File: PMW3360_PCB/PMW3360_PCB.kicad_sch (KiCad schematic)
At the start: 15 parts, among them J1 Conn_01x08, U1 PMW3360DM-T2QU, U2 TPS73601DBV

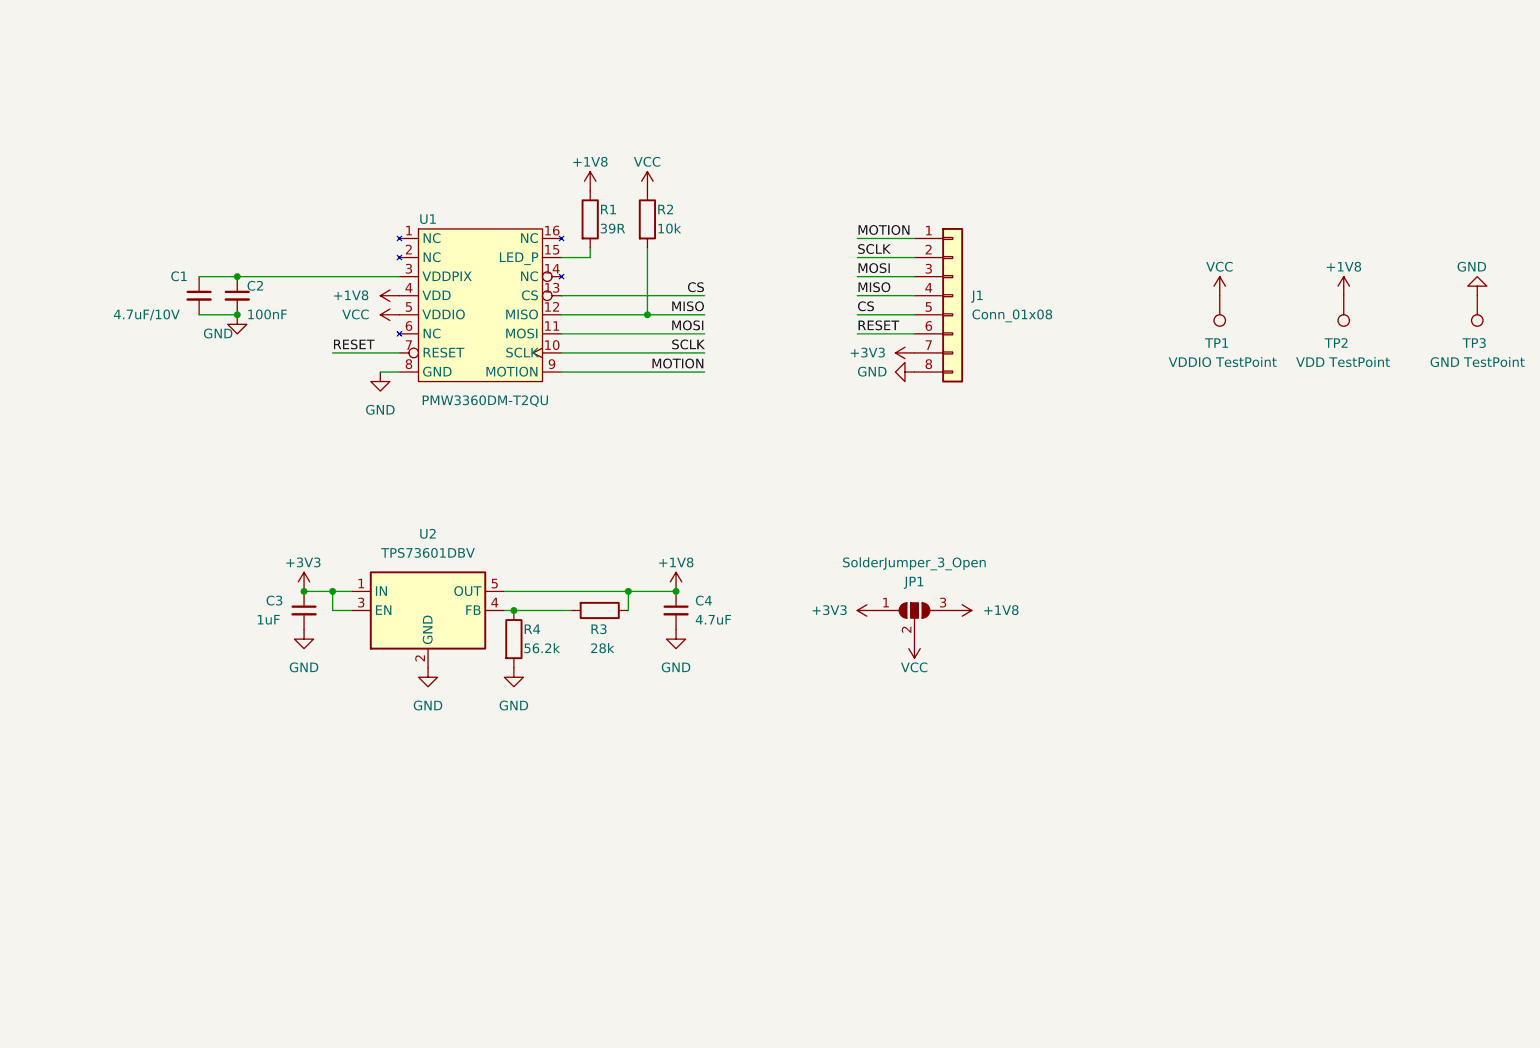
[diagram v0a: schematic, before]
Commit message: Update power net name
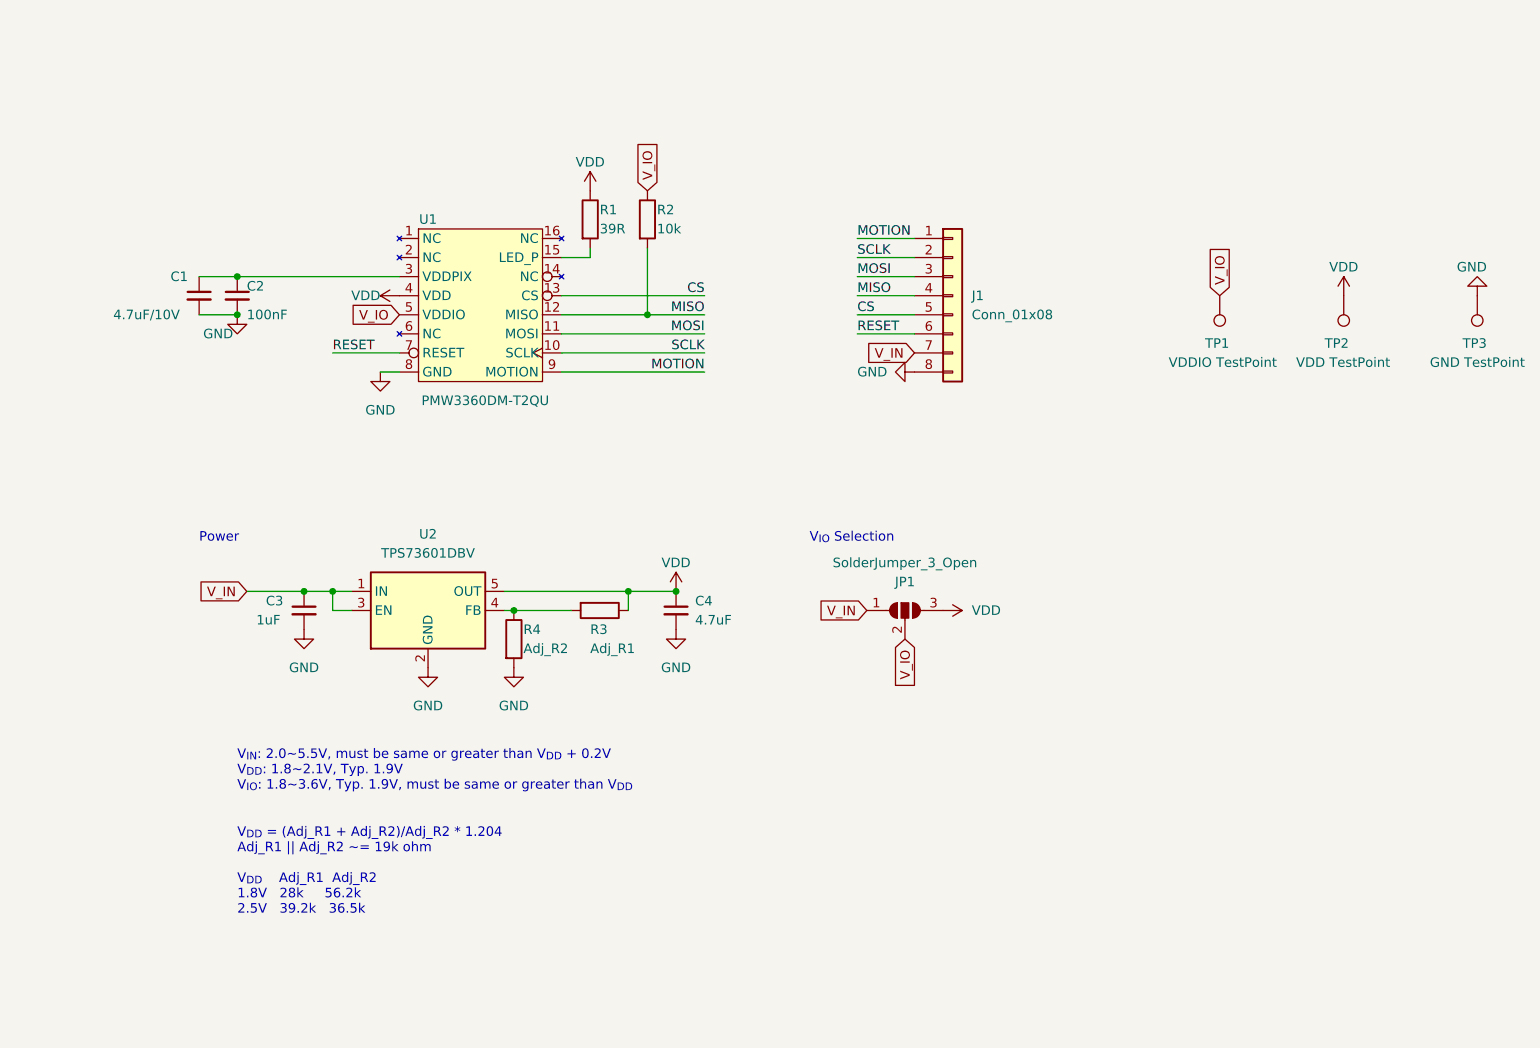
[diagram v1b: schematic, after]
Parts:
- R3: value 28k -> Adj_R1
- R4: value 56.2k -> Adj_R2
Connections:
- net +1V8 renamed VDD
- net +3V3 renamed V_IN
- net VCC renamed V_IO
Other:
- note added: "Power"
- note added: "V_{DD} = (Adj_R1 + Adj_R2)/Adj_R2 * 1.204 Adj_R1 || Adj_R2 ~= 19k ohm V_{DD} Adj_R1 Adj_R2 1.8V 28k 56.2k 2.5V 39.2k 36.5k"
- note added: "V_{IN}: 2.0~5.5V, must be same or greater than V_{DD} + 0.2V V_{DD}: 1.8~2.1V, Typ. 1.9V V_{IO}: 1.8~3.6V, Typ. 1.9V, must be same or greater than V_{DD}"
- note added: "V_{IO} Selection"
- moved on the sheet: JP1

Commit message: Update 2.1
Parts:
- TP1: value VDDIO TestPoint -> VIO TestPoint
- U1: footprint PMW3360_PCB:16pin‐DIP(PMW3360DM-T2QU) -> PMW3360_PCB:PMW3360DM-T2QU 16Pin
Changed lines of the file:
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@@
   (title_block
     (title "PMW3360 PCB")
-    (date "2022-10-14")
-    (rev "2.0")
+    (date "2022-10-17")
+    (rev "2.1")
     (comment 1 "PMW3360DM-T2QU optical mouse sensor breakout board")
     (comment 2 "MIT License, Open Source Hardware")
@@
       (effects (font (size 1.27 1.27)) (justify left))
     )
-    (property "Value" "VDDIO TestPoint" (id 1) (at 217.17 78.74 0)
+    (property "Value" "VIO TestPoint" (id 1) (at 217.17 78.74 0)
       (effects (font (size 1.27 1.27)) (justify left))
     )
@@
     (property "Reference" "U1" (id 0) (at 104.14 59.69 0))
     (property "Value" "PMW3360DM-T2QU" (id 1) (at 111.76 83.82 0))
-    (property "Footprint" "PMW3360_PCB:16pin‐DIP(PMW3360DM-T2QU)" (id 2) (at 105.41 69.85 0)
+    (property "Footprint" "PMW3360_PCB:PMW3360DM-T2QU 16Pin" (id 2) (at 105.41 69.85 0)
       (effects (font (size 1.27 1.27)) hide)
     )
@@
     )
     (path "/492ff555-b5b4-427f-8264-7208174413ab"
-      (reference "TP1") (unit 1) (value "VDDIO TestPoint") (footprint "TestPoint:TestPoint_Pad_D1.5mm")
+      (reference "TP1") (unit 1) (value "VIO TestPoint") (footprint "TestPoint:TestPoint_Pad_D1.5mm")
     )
     (path "/2b2454b4-a75e-470e-b3d6-7aecc9f1ad03"
@@
     )
     (path "/4e369f56-4caf-4dde-9d82-7f50a5c4373c"
-      (reference "U1") (unit 1) (value "PMW3360DM-T2QU") (footprint "PMW3360_PCB:16pin‐DIP(PMW3360DM-T2QU)")
+      (reference "U1") (unit 1) (value "PMW3360DM-T2QU") (footprint "PMW3360_PCB:PMW3360DM-T2QU 16Pin")
     )
     (path "/983f3216-a047-41a8-9fa2-233d2d094141"

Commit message: Update Rev 3.0
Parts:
- added H1, H2, H3, H4: MountingHole_Pad, MountingHole:MountingHole_2.2mm_M2_ISO14580_Pad, symbol Mechanical:MountingHole_Pad
- added R3: DNI, Resistor_SMD:R_0603_1608Metric_Pad0.98x0.95mm_HandSolder, symbol Device:R
- J1: footprint Connector_PinHeader_2.54mm:PinHeader_1x08_P2.54mm_Vertical -> Connector_JST:JST_GH_SM08B-GHS-TB_1x08-1MP_P1.25mm_Horizontal
- renumbered R3 to R4, R4 to R5
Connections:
- net CS: now also J1.6 (Pin_6); no longer J1.5 (Pin_5)
- net GND: now also H1.1, H2.1, H3.1, H4.1
- net MISO: now also J1.5 (Pin_5); no longer J1.4 (Pin_4)
- net MOSI: now also J1.4 (Pin_4); no longer J1.3 (Pin_3)
- net MOTION: now also J1.2 (Pin_2); no longer J1.1 (Pin_1)
- net RESET: now also J1.1 (Pin_1), R3.2; no longer J1.6 (Pin_6)
- net SCLK: now also J1.3 (Pin_3); no longer J1.2 (Pin_2)
- net V_IO: now also R3.1
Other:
- moved on the sheet: C1, C2, C3, C4, J1, JP1

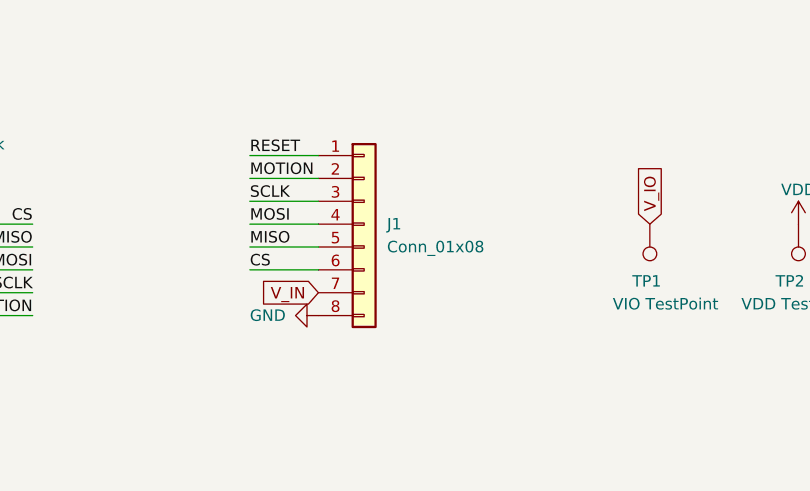
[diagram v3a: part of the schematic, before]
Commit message: Replace JST GH 1.25 connector with 0.5mm FPC
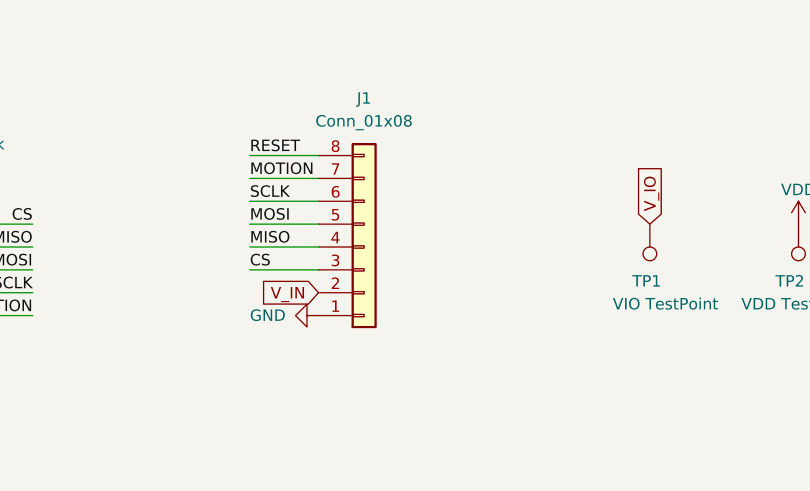
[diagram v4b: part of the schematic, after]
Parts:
- J1: footprint Connector_JST:JST_GH_SM08B-GHS-TB_1x08-1MP_P1.25mm_Horizontal -> ErgoSNM_Keyboard:FPC_8P_0.5mm_AFC01-S08FCA-00
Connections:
- net CS: now also J1.3 (Pin_3); no longer J1.6 (Pin_6)
- net GND: now also J1.1 (Pin_1); no longer J1.8 (Pin_8)
- net MISO: now also J1.4 (Pin_4); no longer J1.5 (Pin_5)
- net MOSI: now also J1.5 (Pin_5); no longer J1.4 (Pin_4)
- net MOTION: now also J1.7 (Pin_7); no longer J1.2 (Pin_2)
- net RESET: now also J1.8 (Pin_8); no longer J1.1 (Pin_1)
- net SCLK: now also J1.6 (Pin_6); no longer J1.3 (Pin_3)
- net V_IN: now also J1.2 (Pin_2); no longer J1.7 (Pin_7)
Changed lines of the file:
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@@
   (title_block
     (title "PMW3360 PCB")
-    (date "2022-12-27")
-    (rev "3.0")
+    (date "2023-02-26")
+    (rev "3.1")
     (comment 1 "PMW3360DM-T2QU optical mouse sensor breakout board")
     (comment 2 "MIT License, Open Source Hardware")
@@
     (stroke (width 0) (type default) (color 0 0 0 0))
   )
+  (wire (pts (xy 165.1 74.93) (xy 172.72 74.93))
+    (stroke (width 0) (type default) (color 0 0 0 0))
+  )
   (wire (pts (xy 78.74 77.47) (xy 87.63 77.47))
     (stroke (width 0) (type default) (color 0 0 0 0))
@@
     (stroke (width 0) (type default) (color 0 0 0 0))
   )
+  (wire (pts (xy 165.1 67.31) (xy 172.72 67.31))
+    (stroke (width 0) (type default) (color 0 0 0 0))
+  )
   (wire (pts (xy 115.57 111.76) (xy 114.3 111.76))
     (stroke (width 0) (type default) (color 0 0 0 0))
   )
-  (wire (pts (xy 165.1 74.93) (xy 172.72 74.93))
+  (wire (pts (xy 130.81 109.22) (xy 130.81 111.76))
+    (stroke (width 0) (type default) (color 0 0 0 0))
+  )
+  (wire (pts (xy 165.1 62.23) (xy 172.72 62.23))
+    (stroke (width 0) (type default) (color 0 0 0 0))
+  )
+  (wire (pts (xy 121.92 74.93) (xy 140.97 74.93))
+    (stroke (width 0) (type default) (color 0 0 0 0))
+  )
+  (wire (pts (xy 62.23 72.39) (xy 64.77 72.39))
+    (stroke (width 0) (type default) (color 0 0 0 0))
+  )
+  (wire (pts (xy 62.23 67.31) (xy 67.31 67.31))
+    (stroke (width 0) (type default) (color 0 0 0 0))
+  )
+  (wire (pts (xy 80.01 109.22) (xy 87.63 109.22))
+    (stroke (width 0) (type default) (color 0 0 0 0))
+  )
+  (wire (pts (xy 87.63 77.47) (xy 100.33 77.47))
+    (stroke (width 0) (type default) (color 0 0 0 0))
+  )
+  (wire (pts (xy 130.81 109.22) (xy 137.16 109.22))
     (stroke (width 0) (type default) (color 0 0 0 0))
   )
@@
     (stroke (width 0) (type default) (color 0 0 0 0))
   )
-  (wire (pts (xy 130.81 109.22) (xy 130.81 111.76))
-    (stroke (width 0) (type default) (color 0 0 0 0))
-  )
-  (wire (pts (xy 165.1 67.31) (xy 172.72 67.31))
-    (stroke (width 0) (type default) (color 0 0 0 0))
-  )
-  (wire (pts (xy 121.92 74.93) (xy 140.97 74.93))
+  (wire (pts (xy 97.79 80.01) (xy 100.33 80.01))
+    (stroke (width 0) (type default) (color 0 0 0 0))
+  )
+  (wire (pts (xy 64.77 72.39) (xy 67.31 72.39))
+    (stroke (width 0) (type default) (color 0 0 0 0))
+  )
+  (wire (pts (xy 123.19 111.76) (xy 115.57 111.76))
+    (stroke (width 0) (type default) (color 0 0 0 0))
+  )
+  (wire (pts (xy 165.1 72.39) (xy 172.72 72.39))
+    (stroke (width 0) (type default) (color 0 0 0 0))
+  )
+  (wire (pts (xy 121.92 77.47) (xy 140.97 77.47))
+    (stroke (width 0) (type default) (color 0 0 0 0))
+  )
+  (wire (pts (xy 93.98 111.76) (xy 91.44 111.76))
+    (stroke (width 0) (type default) (color 0 0 0 0))
+  )
+  (wire (pts (xy 87.63 111.76) (xy 87.63 109.22))
+    (stroke (width 0) (type default) (color 0 0 0 0))
+  )
+  (wire (pts (xy 137.16 111.76) (xy 137.16 109.22))
+    (stroke (width 0) (type default) (color 0 0 0 0))
+  )
+  (wire (pts (xy 121.92 80.01) (xy 140.97 80.01))
+    (stroke (width 0) (type default) (color 0 0 0 0))
+  )
+  (wire (pts (xy 121.92 72.39) (xy 133.35 72.39))
+    (stroke (width 0) (type default) (color 0 0 0 0))
+  )
+  (wire (pts (xy 133.35 72.39) (xy 140.97 72.39))
+    (stroke (width 0) (type default) (color 0 0 0 0))
+  )
+  (wire (pts (xy 121.92 69.85) (xy 140.97 69.85))
+    (stroke (width 0) (type default) (color 0 0 0 0))
+  )
+  (wire (pts (xy 67.31 67.31) (xy 100.33 67.31))
     (stroke (width 0) (type default) (color 0 0 0 0))
   )
@@
     (stroke (width 0) (type default) (color 0 0 0 0))
   )
-  (wire (pts (xy 62.23 72.39) (xy 64.77 72.39))
-    (stroke (width 0) (type default) (color 0 0 0 0))
-  )
-  (wire (pts (xy 62.23 67.31) (xy 67.31 67.31))
-    (stroke (width 0) (type default) (color 0 0 0 0))
-  )
-  (wire (pts (xy 80.01 109.22) (xy 87.63 109.22))
-    (stroke (width 0) (type default) (color 0 0 0 0))
-  )
-  (wire (pts (xy 165.1 62.23) (xy 172.72 62.23))
-    (stroke (width 0) (type default) (color 0 0 0 0))
-  )
-  (wire (pts (xy 87.63 77.47) (xy 100.33 77.47))
-    (stroke (width 0) (type default) (color 0 0 0 0))
-  )
-  (wire (pts (xy 130.81 109.22) (xy 137.16 109.22))
-    (stroke (width 0) (type default) (color 0 0 0 0))
-  )
-  (wire (pts (xy 97.79 80.01) (xy 100.33 80.01))
-    (stroke (width 0) (type default) (color 0 0 0 0))
-  )
-  (wire (pts (xy 64.77 72.39) (xy 67.31 72.39))
-    (stroke (width 0) (type default) (color 0 0 0 0))
-  )
-  (wire (pts (xy 123.19 111.76) (xy 115.57 111.76))
-    (stroke (width 0) (type default) (color 0 0 0 0))
-  )
-  (wire (pts (xy 121.92 77.47) (xy 140.97 77.47))
-    (stroke (width 0) (type default) (color 0 0 0 0))
-  )
-  (wire (pts (xy 93.98 111.76) (xy 91.44 111.76))
-    (stroke (width 0) (type default) (color 0 0 0 0))
-  )
-  (wire (pts (xy 87.63 111.76) (xy 87.63 109.22))
-    (stroke (width 0) (type default) (color 0 0 0 0))
-  )
-  (wire (pts (xy 137.16 111.76) (xy 137.16 109.22))
-    (stroke (width 0) (type default) (color 0 0 0 0))
-  )
-  (wire (pts (xy 121.92 80.01) (xy 140.97 80.01))
-    (stroke (width 0) (type default) (color 0 0 0 0))
-  )
-  (wire (pts (xy 121.92 72.39) (xy 133.35 72.39))
-    (stroke (width 0) (type default) (color 0 0 0 0))
-  )
-  (wire (pts (xy 133.35 72.39) (xy 140.97 72.39))
-    (stroke (width 0) (type default) (color 0 0 0 0))
-  )
-  (wire (pts (xy 121.92 69.85) (xy 140.97 69.85))
-    (stroke (width 0) (type default) (color 0 0 0 0))
-  )
-  (wire (pts (xy 67.31 67.31) (xy 100.33 67.31))
-    (stroke (width 0) (type default) (color 0 0 0 0))
-  )
   (wire (pts (xy 121.92 64.77) (xy 125.73 64.77))
-    (stroke (width 0) (type default) (color 0 0 0 0))
-  )
-  (wire (pts (xy 165.1 72.39) (xy 172.72 72.39))
     (stroke (width 0) (type default) (color 0 0 0 0))
   )
@@
     (pin "3")
   )
-  (symbol (lib_id "Connector_Generic:Conn_01x08") (at 177.8 69.85 0) (unit 1)
+  (symbol (lib_id "Connector_Generic:Conn_01x08") (at 177.8 72.39 0) (mirror x) (unit 1)
     (in_bom yes) (on_board yes) (fields_autoplaced)
-    (property "Reference" "J1" (id 0) (at 180.34 69.8499 0)
-      (effects (font (size 1.27 1.27)) (justify left))
-    )
-    (property "Value" "Conn_01x08" (id 1) (at 180.34 72.3899 0)
-      (effects (font (size 1.27 1.27)) (justify left))
-    )
-    (property "Footprint" "Connector_JST:JST_GH_SM08B-GHS-TB_1x08-1MP_P1.25mm_Horizontal" (id 2) (at 177.8 69.85 0)
-      (effects (font (size 1.27 1.27)) hide)
-    )
-    (property "Datasheet" "~" (id 3) (at 177.8 69.85 0)
+    (property "Reference" "J1" (id 0) (at 177.8 55.88 0))
+    (property "Value" "Conn_01x08" (id 1) (at 177.8 58.42 0))
+    (property "Footprint" "ErgoSNM_Keyboard:FPC_8P_0.5mm_AFC01-S08FCA-00" (id 2) (at 177.8 72.39 0)
+      (effects (font (size 1.27 1.27)) hide)
+    )
+    (property "Datasheet" "~" (id 3) (at 177.8 72.39 0)
       (effects (font (size 1.27 1.27)) hide)
     )
@@
     )
     (path "/e0ae36e1-f2bd-4988-b227-24022925bf63"
-      (reference "J1") (unit 1) (value "Conn_01x08") (footprint "Connector_JST:JST_GH_SM08B-GHS-TB_1x08-1MP_P1.25mm_Horizontal")
+      (reference "J1") (unit 1) (value "Conn_01x08") (footprint "ErgoSNM_Keyboard:FPC_8P_0.5mm_AFC01-S08FCA-00")
     )
     (path "/df4b2fe5-29f6-40cc-9d1c-e703b4cb57c5"
